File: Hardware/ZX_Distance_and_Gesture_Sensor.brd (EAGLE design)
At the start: 160 x 100 mm, 42 parts, among them Q1 MMBT2222A, Q2 MOSFET-NCHANNEL2N7002PW

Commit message: Placed components on PCB and started layout
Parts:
- D1, D2: value SFH4641 -> SFH4641LARGE
- moved U$5 137.5 mm to (36.8, 16.5)
- moved STANDOFF2 127.6 mm to (25.4, 0.00)
- moved LOGO1 124.8 mm to (22.2, 2.54)
- moved FID2 119.4 mm to (22.9, -5.08)
- moved FRAME1 81.9 mm to (-6.35, -19.1)
- moved LOGO2 77.9 mm to (-23.5, -3.81)
- moved R10 77.3 mm to (6.35, -5.08), turned to 180 degrees
- moved C6 76.8 mm to (15.2, -3.81), turned to 270 degrees
- moved STANDOFF1 76.8 mm to (-25.4, 0.00)
- moved R8 75.5 mm to (12.7, -3.81), turned to 270 degrees
- moved FID1 73.9 mm to (-22.9, 5.08)
- moved R11 71.9 mm to (-5.08, -5.08)
- moved R7 71.9 mm to (10.2, -5.08)
- moved C7 70.9 mm to (2.54, -5.08)
- moved C8 70.9 mm to (5.08, 2.54)
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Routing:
- net VCC: track 0.00 -> 52.0 mm, vias 0 -> 4
- net N$9: track 0.00 -> 15.9 mm
- net EM2: track 0.00 -> 15.6 mm, vias 0 -> 2
- net COMMON: track 0.00 -> 15.1 mm, vias 0 -> 2
- net N$12: track 0.00 -> 12.4 mm, vias 0 -> 2
- net I2C_ADDR: track 0.00 -> 11.0 mm, vias 0 -> 1
- net ICSPCLK: track 0.00 -> 10.1 mm, vias 0 -> 1
- net CARRIER: track 0.00 -> 9.44 mm, vias 0 -> 1
- net I2C_SDA: track 0.00 -> 8.24 mm
- net I2C_SCL: track 0.00 -> 7.95 mm, vias 0 -> 1
- net ICSPDAT: track 0.00 -> 7.17 mm, vias 0 -> 1
- net N$4: track 0.00 -> 6.50 mm
- net N$5: track 0.00 -> 4.49 mm
- net RECEIVER: track 0.00 -> 3.08 mm, vias 0 -> 1
- net N$11: track 0.00 -> 2.71 mm
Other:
- board size 160 x 100 mm -> 55.9 x 15.4 mm
- board text added: "Shawn Hymel in collaboration with XYZ Interactive Technologies"

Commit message: More progress on layout
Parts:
- D1, D2: value SFH4641LARGE -> SFH4641OVERSIZE; device SparkFun-LED:SFH4641 -> SparkFun-LED:SFH4641-OVERSIZE
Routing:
- net COMMON: track 15.1 -> 44.2 mm
- net VCC: track 52.0 -> 54.7 mm, vias 4 -> 5
- net EM1: track 0.00 -> 1.92 mm, vias 0 -> 1
- net I2C_SCL: track 7.95 -> 8.54 mm

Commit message: Almost done with layout
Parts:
- moved Q1 7.73 mm to (-14.0, 3.81), turned to 90 degrees
- moved C4 4.02 mm to (-14.0, -3.81)
- moved U$3 4.02 mm to (-15.2, 0.00), turned to 180 degrees
- moved SJ1 1.27 mm to (-2.54, -5.08)
- moved C3 1.27 mm to (-11.4, 0.00)
- moved R11 1.27 mm to (-6.35, -5.08)
- turned C1 to 270 degrees
- turned C5 to 90 degrees
- turned R7 to 180 degrees
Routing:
- net VCC: track 54.7 -> 97.6 mm, vias 5 -> 6
- net N$2: track 0.00 -> 24.3 mm, vias 0 -> 3
- net COMMON: track 44.2 -> 64.7 mm, vias 2 -> 4
- net EM1: track 1.92 -> 20.5 mm, vias 1 -> 2
- net RECEIVER: track 2.96 -> 21.4 mm, vias 1 -> 3
- net N$7: track 0.00 -> 18.0 mm, vias 0 -> 2
- net UART_TX: track 0.00 -> 16.7 mm, vias 0 -> 1
- net I2C_SCL: track 8.54 -> 23.9 mm, vias 1 -> 2
- net N$8: track 0.00 -> 14.9 mm, vias 0 -> 2
- net N$6: track 0.00 -> 13.3 mm, vias 0 -> 2
- net GND: track 0.00 -> 13.0 mm, vias 0 -> 30
- net N$1: track 0.00 -> 12.7 mm
- net UART_RX: track 0.00 -> 12.5 mm, vias 0 -> 1
- net MCLR: track 0.00 -> 10.3 mm, vias 0 -> 1
- net N$10: track 0.00 -> 9.39 mm
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- added copper zone on layer 1, net GND
- added copper zone on layer 16, net GND

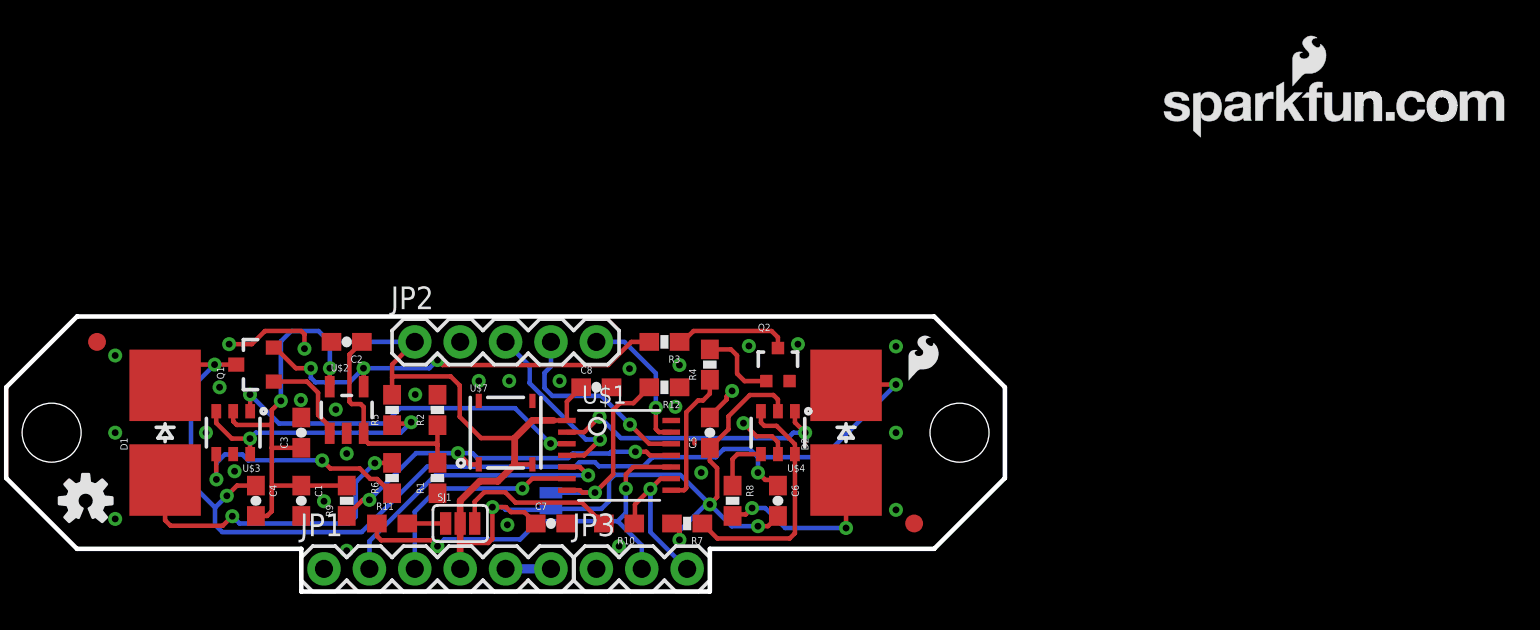
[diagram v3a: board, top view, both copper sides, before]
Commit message: Completed layout. Ready for review before prototype.
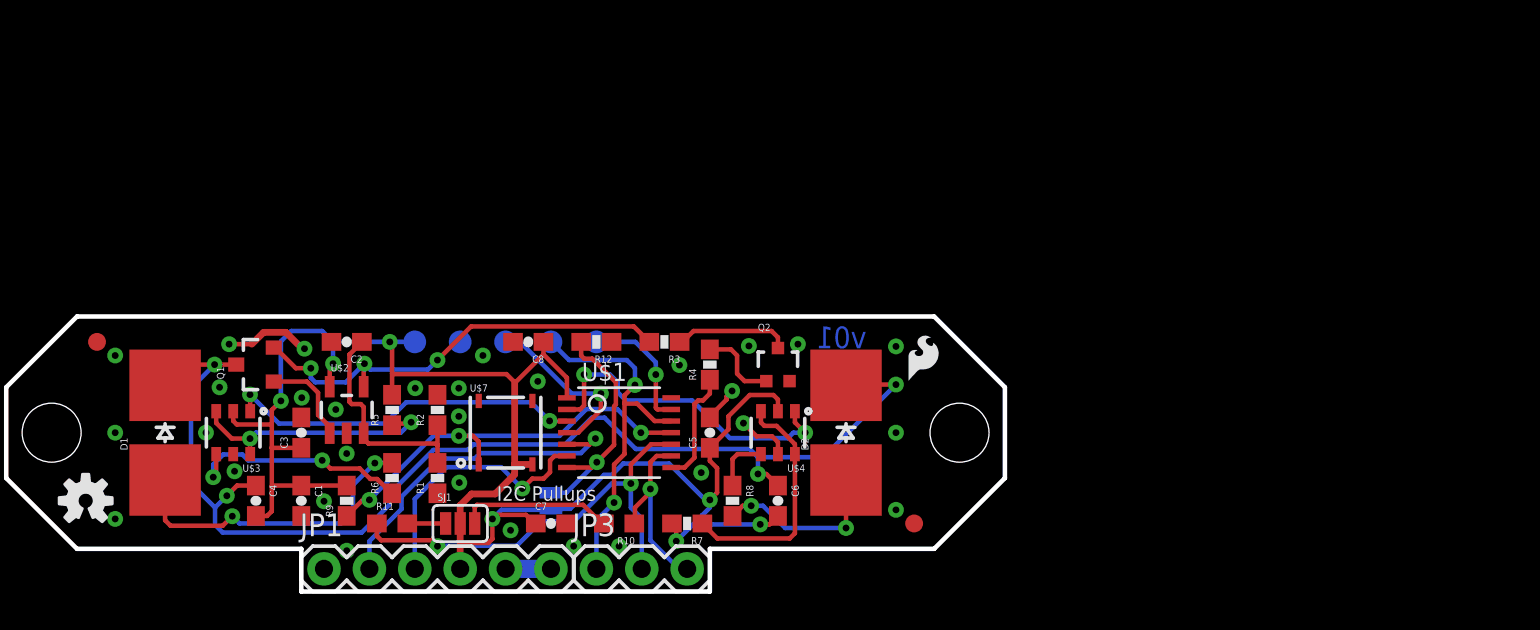
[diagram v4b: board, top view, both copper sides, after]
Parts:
- removed JP2: (no value), SparkFun-Connectors:1X05
- added TP1, TP2, TP3, TP4, TP5: TEST-POINT3X5, SparkFun-Passives:PAD.03X.05
- U$5: value SFE_LOGO_NAME_WEB -> SFE_LOGO_NAME_FLAME.1_INCH; device SparkFun-Aesthetics:SFE-NEW-WEBLOGO -> SparkFun-Aesthetics:SFE_LOGO_NAME_FLAME_.1
- moved U$5 62.9 mm to (-22.0, -5.84), flipped to the bottom, turned to 90 degrees
- moved FRAME1 19.1 mm to (-25.4, -17.8)
- moved R12 4.58 mm to (5.08, 5.08)
- moved C8 4.58 mm to (1.27, 5.08), turned to 180 degrees
- moved U$1 1.27 mm to (6.35, 0.00)
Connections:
- removed net DATA_RDY: JP3.1
- removed net ICSPCLK: JP2.4, U$1.12
- new net ICSPCLK/DATA_RDY: JP3.1, TP4.P$1, U$1.12
- net GND: now also TP2.P$1; no longer JP2.2
- net ICSPDAT: now also TP5.P$1; no longer JP2.5
- net MCLR: now also TP3.P$1; no longer JP2.3
- net VCC: now also TP1.P$1; no longer JP2.1
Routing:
- net ICSPCLK/DATA_RDY: track 0.00 -> 20.5 mm, vias 0 -> 2
- net ICSPCLK: track 11.1 -> 0.00 mm, vias 1 -> 0
- net EM2: track 15.7 -> 18.5 mm
- net UART_RX: track 12.5 -> 14.8 mm
- net RECEIVER: track 21.4 -> 23.7 mm
- net COMMON: track 64.7 -> 66.8 mm
- net UART_TX: track 16.7 -> 18.7 mm
- net I2C_SDA: track 9.07 -> 10.8 mm
- net I2C_ADDR: track 11.7 -> 13.3 mm
- net I2C_SCL: track 23.9 -> 25.4 mm
- net CARRIER: track 7.66 -> 6.41 mm
- net N$2: track 24.3 -> 25.4 mm
- net ICSPDAT: track 8.11 -> 7.24 mm
- net N$10: track 9.39 -> 8.72 mm
- net GND: track 13.0 -> 12.5 mm, vias 30 -> 31
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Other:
- board text added: "CL"
- board text added: "DA"
- board text added: "DR"
- board text added: "GND"
- board text added: "I2C"
- board text added: "I2C Pullups"
- board text added: "Op: 0x20 Cl: 0x22"
- board text added: "RX"
- board text added: "TX"
- board text added: "UART"
- board text added: "VCC"
- board text added: "ZX Sensor"
- board text added: "v01"

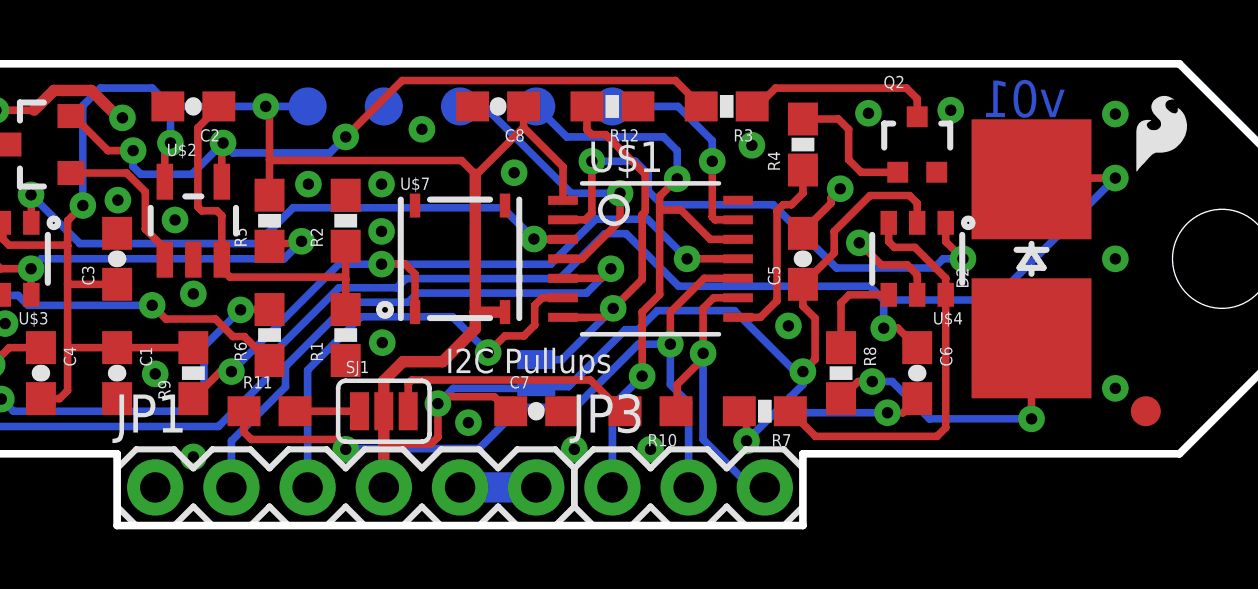
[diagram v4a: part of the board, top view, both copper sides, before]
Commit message: Added trace to DACOUT line. Made test point programming pads smaller. Added extra via on GND plane to beef up current carrying capability.
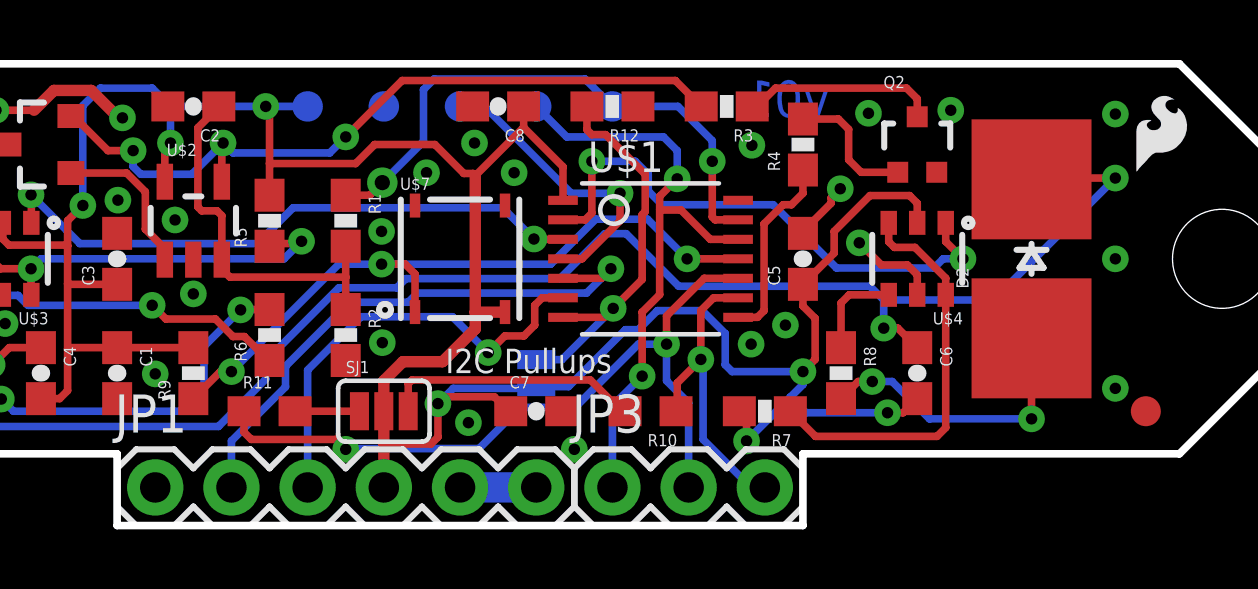
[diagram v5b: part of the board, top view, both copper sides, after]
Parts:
- TP1, TP2, TP3, TP4, TP5: value TEST-POINT3X5 -> TEST-POINT3X4; device SparkFun-Passives:PAD.03X.05 -> SparkFun-Passives:PAD.03X.04
- moved R1 3.81 mm to (-3.81, 1.27), turned to 270 degrees
- moved R2 3.81 mm to (-3.81, -2.54), turned to 270 degrees
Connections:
- removed net DACOUT: R1.1
- removed net ICSPDAT: TP5.P$1, U$1.13
- new net ICSPDAT/DACOUT: R1.1, TP5.P$1, U$1.13
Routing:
- net ICSPDAT/DACOUT: track 0.00 -> 19.2 mm, vias 0 -> 2
- net ICSPDAT: track 7.24 -> 0.00 mm, vias 1 -> 0
- net VCC: track 98.1 -> 99.4 mm
- net GND: vias 31 -> 29
